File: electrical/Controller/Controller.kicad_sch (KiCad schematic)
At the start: 30 parts, among them J1 USB4145-03-0170-C, J3 TC2030-NL, U1 LP5912-3.3DRV, U2 USBLC6-2P6, U3 STM32L072CBTx

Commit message: Fix part selection for i2c pull-ups
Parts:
- R5, R6: LCSC C22939 -> C4190; Part UNI-ROYAL 0603WAF220KT5E -> UNI-ROYAL 0603WAF2201T5E
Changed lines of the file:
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@@
 			)
 		)
-		(property "Datasheet" "https://www.lcsc.com/datasheet/C22939.pdf"
+		(property "Datasheet" "https://www.lcsc.com/datasheet/C4190.pdf"
 			(at 281.94 149.86 0)
 			(effects
@@
 			)
 		)
-		(property "LCSC" "C22939"
+		(property "LCSC" "C4190"
 			(at 281.94 149.86 0)
 			(effects
@@
 			)
 		)
-		(property "Part" "UNI-ROYAL 0603WAF220KT5E"
+		(property "Part" "UNI-ROYAL 0603WAF2201T5E"
 			(at 281.94 149.86 0)
 			(effects
@@
 			)
 		)
-		(property "Datasheet" "https://www.lcsc.com/datasheet/C22939.pdf"
+		(property "Datasheet" "https://www.lcsc.com/datasheet/C4190.pdf"
 			(at 292.1 149.86 0)
 			(effects
@@
 			)
 		)
-		(property "LCSC" "C22939"
+		(property "LCSC" "C4190"
 			(at 292.1 149.86 0)
 			(effects
@@
 			)
 		)
-		(property "Part" "UNI-ROYAL 0603WAF220KT5E"
+		(property "Part" "UNI-ROYAL 0603WAF2201T5E"
 			(at 292.1 149.86 0)
 			(effects

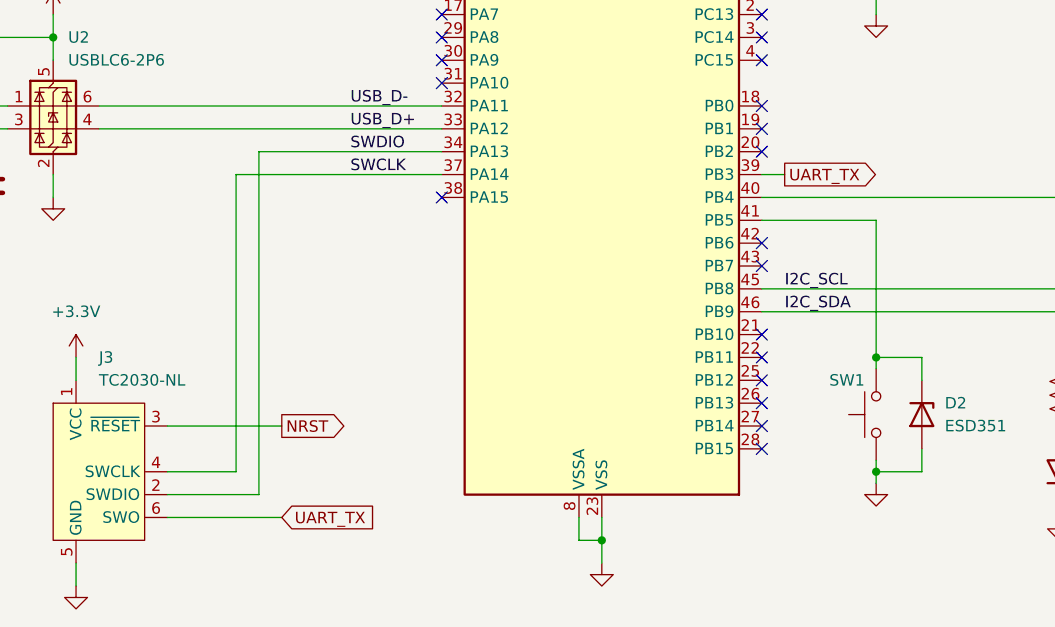
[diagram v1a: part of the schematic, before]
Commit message: Remove UART from debug connector
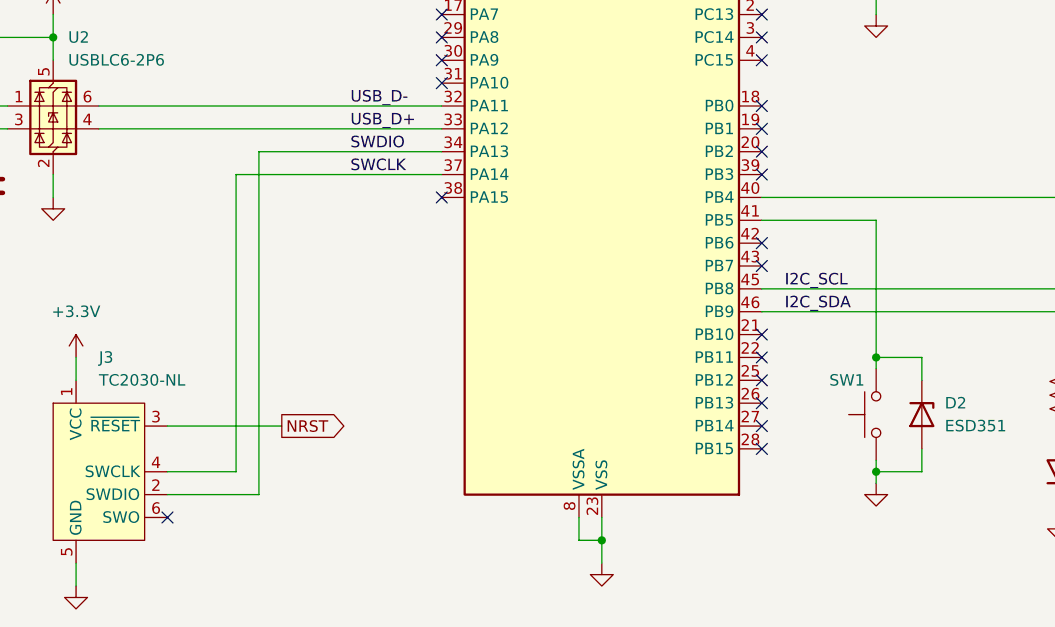
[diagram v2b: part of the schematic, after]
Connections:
- net UART_TX: no longer names the net of U3.39 (PB3)
- net UART_TX: no longer J3.6 (SWO)
- no-connect marks 31 -> 33
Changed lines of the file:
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@@
+	)
+	(no_connect
+		(at 233.68 143.51)
 	)
 	(no_connect
@@
 	)
 	(no_connect
+		(at 167.64 181.61)
+	)
+	(no_connect
 		(at 198.12 120.65)
 	)
@@
 	(wire
 		(pts
-			(xy 180.34 181.61) (xy 167.64 181.61)
-		)
-		(stroke
-			(width 0)
-			(type default)
-		)
-	)
-	(wire
-		(pts
 			(xy 121.92 134.62) (xy 121.92 140.97)
 		)
@@
 		(pts
 			(xy 167.64 171.45) (xy 180.34 171.45)
-		)
-		(stroke
-			(width 0)
-			(type default)
-		)
-	)
-	(wire
-		(pts
-			(xy 236.22 143.51) (xy 233.68 143.51)
 		)
 		(stroke
@@
 		)
 	)
-	(global_label "UART_TX"
-		(shape output)
-		(at 236.22 143.51 0)
-		(fields_autoplaced yes)
-		(effects
-			(font
-				(size 1.27 1.27)
-			)
-			(justify left)
-		)
-		(property "Intersheetrefs" "${INTERSHEET_REFS}"
-			(at 247.0066 143.51 0)
-			(effects
-				(font
-					(size 1.27 1.27)
-				)
-				(justify left)
-				(hide yes)
-			)
-		)
-	)
-	(global_label "UART_TX"
-		(shape input)
-		(at 180.34 181.61 0)
-		(fields_autoplaced yes)
-		(effects
-			(font
-				(size 1.27 1.27)
-			)
-			(justify left)
-		)
-		(property "Intersheetrefs" "${INTERSHEET_REFS}"
-			(at 191.1266 181.61 0)
-			(effects
-				(font
-					(size 1.27 1.27)
-				)
-				(justify left)
-				(hide yes)
-			)
-		)
-	)

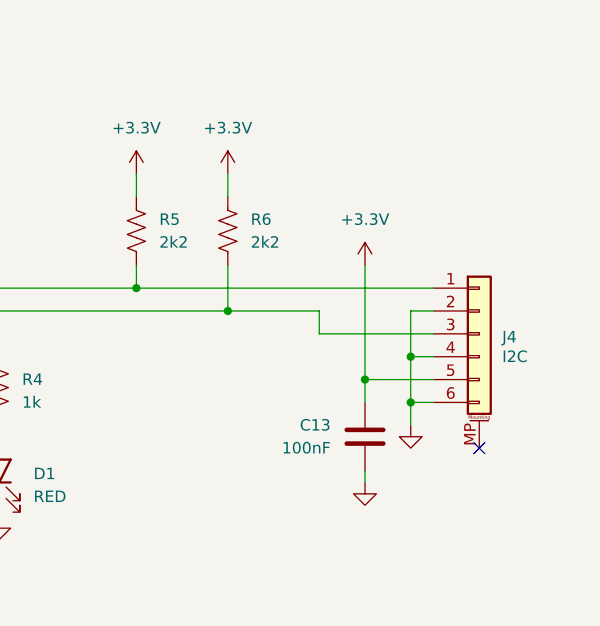
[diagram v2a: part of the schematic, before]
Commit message: Replace PicoBlade connectors with SKEDD
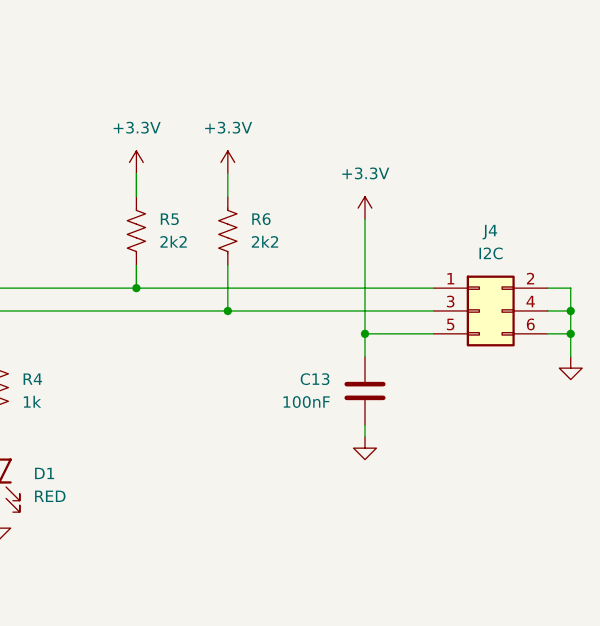
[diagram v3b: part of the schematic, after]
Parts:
- removed J4: ~, Connector_Molex:Molex_PicoBlade_53261-0671_1x06-1MP_P1.25mm_Horizontal, symbol Connector_Generic_MountingPin:Conn_01x06_MountingPin
- added J4: I2C, MidiConcertina:Wuerth_WR-WST_490107670612_2x03_P2.54mm_SKEDD, symbol Connector_Generic:Conn_02x03_Odd_Even
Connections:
- net +3.3V: now also J4.5 (Pin_5)
- net GND: now also J4.2 (Pin_2), J4.4 (Pin_4), J4.6 (Pin_6)
- net I2C_SCL: now also J4.1 (Pin_1)
- net I2C_SDA: now also J4.3 (Pin_3)
- no-connect marks 33 -> 32
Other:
- moved on the sheet: C13

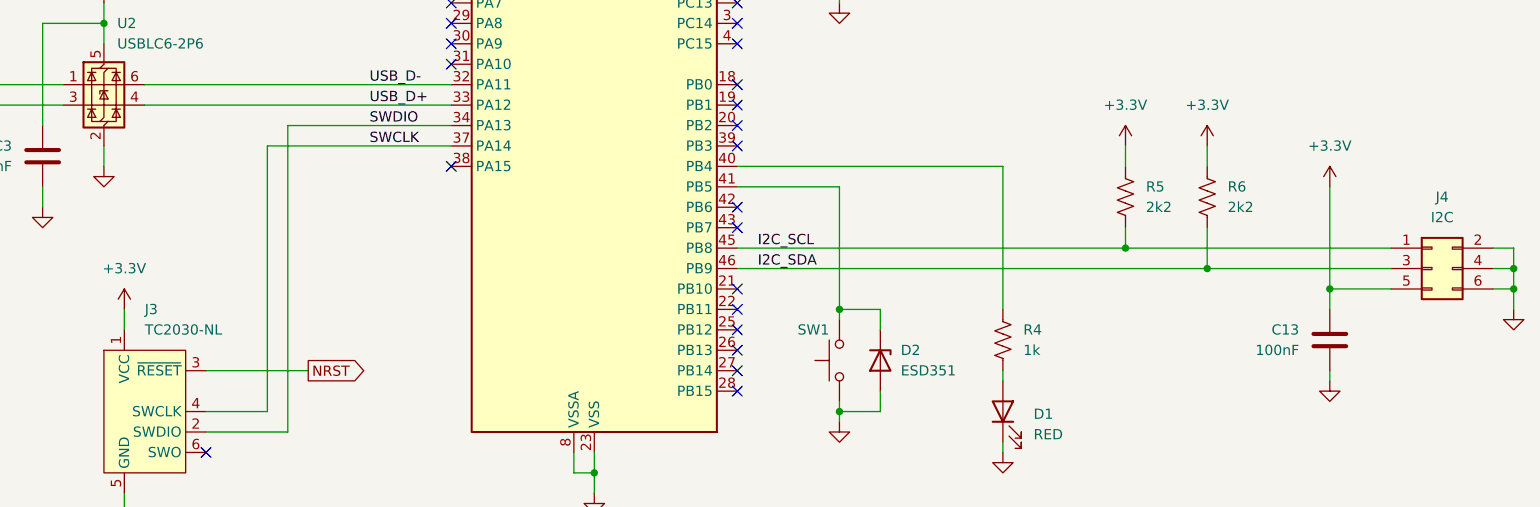
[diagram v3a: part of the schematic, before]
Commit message: Relabel components
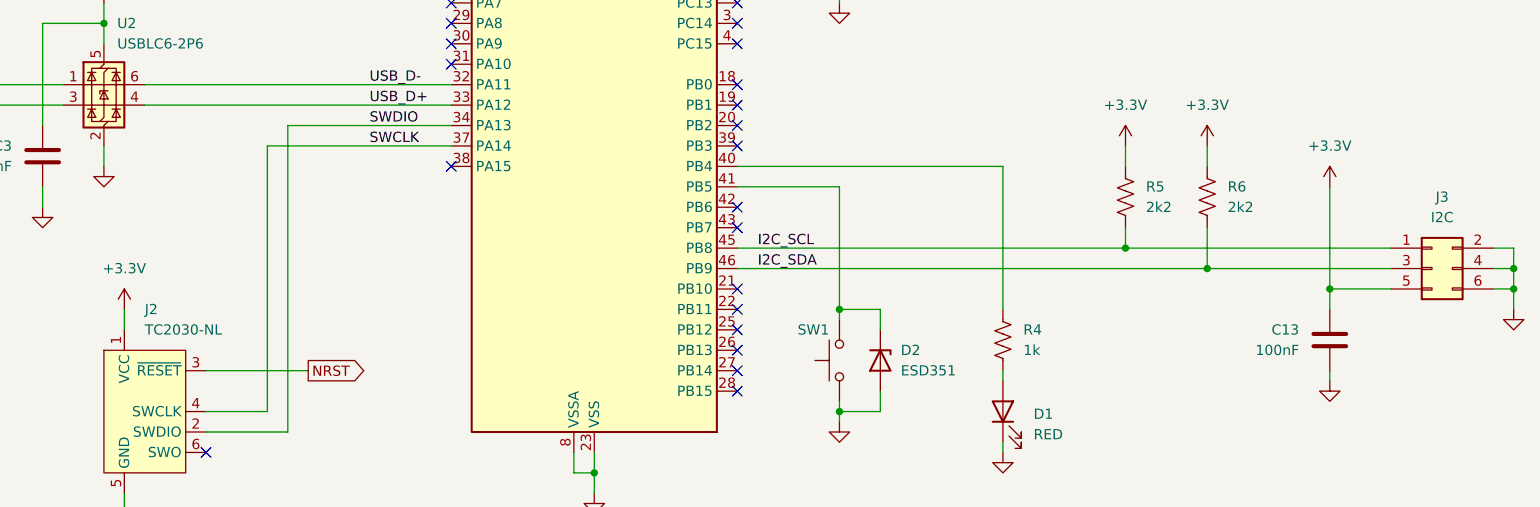
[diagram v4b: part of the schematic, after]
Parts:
- renumbered J3 to J2, J4 to J3
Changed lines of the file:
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@@
 		(dnp no)
 		(fields_autoplaced yes)
-		(property "Reference" "J4"
+		(property "Reference" "J3"
 			(at 321.31 149.86 0)
 			(effects
@@
 			(project ""
 				(path "/da26d94e-7a50-4b99-9678-5aaaf6987a15"
-					(reference "J4")
+					(reference "J3")
 					(unit 1)
 				)
@@
 		(on_board yes)
 		(dnp no)
-		(property "Reference" "J3"
+		(property "Reference" "J2"
 			(at 160.02 163.83 0)
 			(effects
@@
 			(project "control"
 				(path "/da26d94e-7a50-4b99-9678-5aaaf6987a15"
-					(reference "J3")
-					(unit 1)
-				)
+					(reference "J2")
+					(unit 1)
+				)

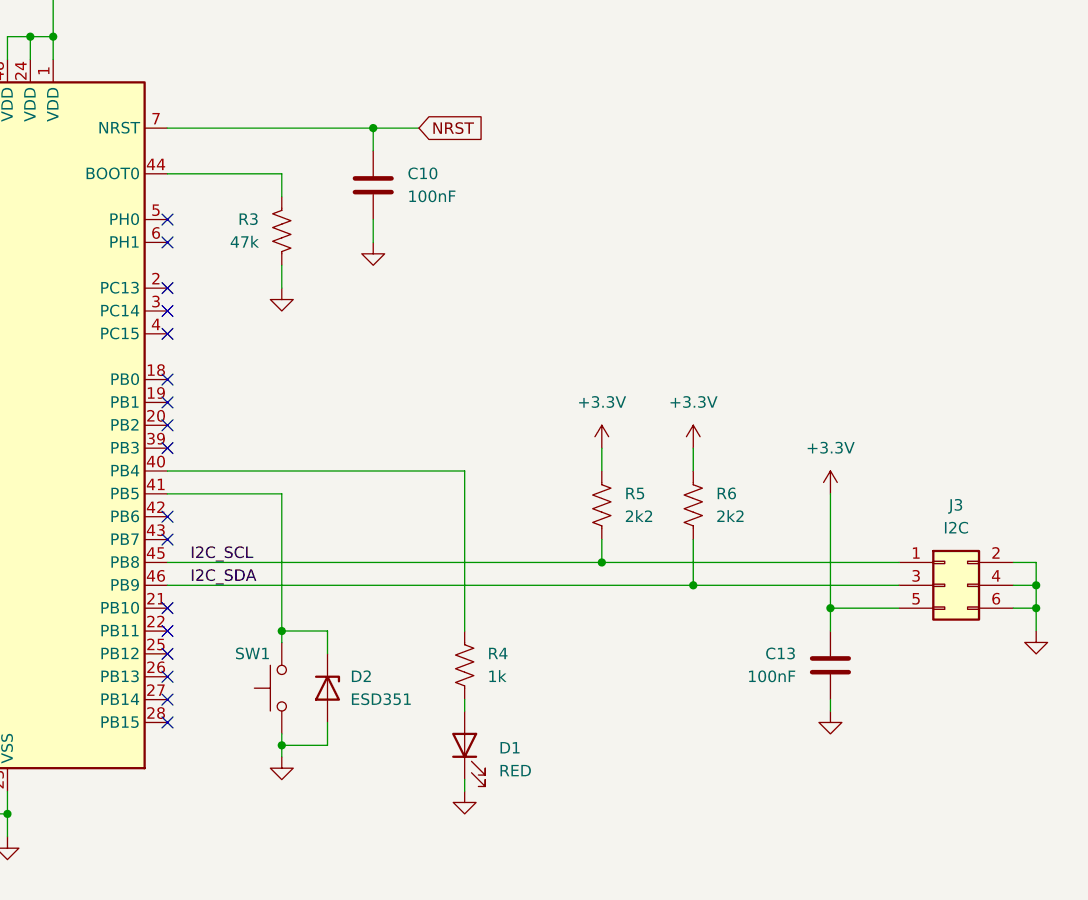
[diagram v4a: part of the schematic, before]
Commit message: Add gpio-controlled switch for i2c bus power
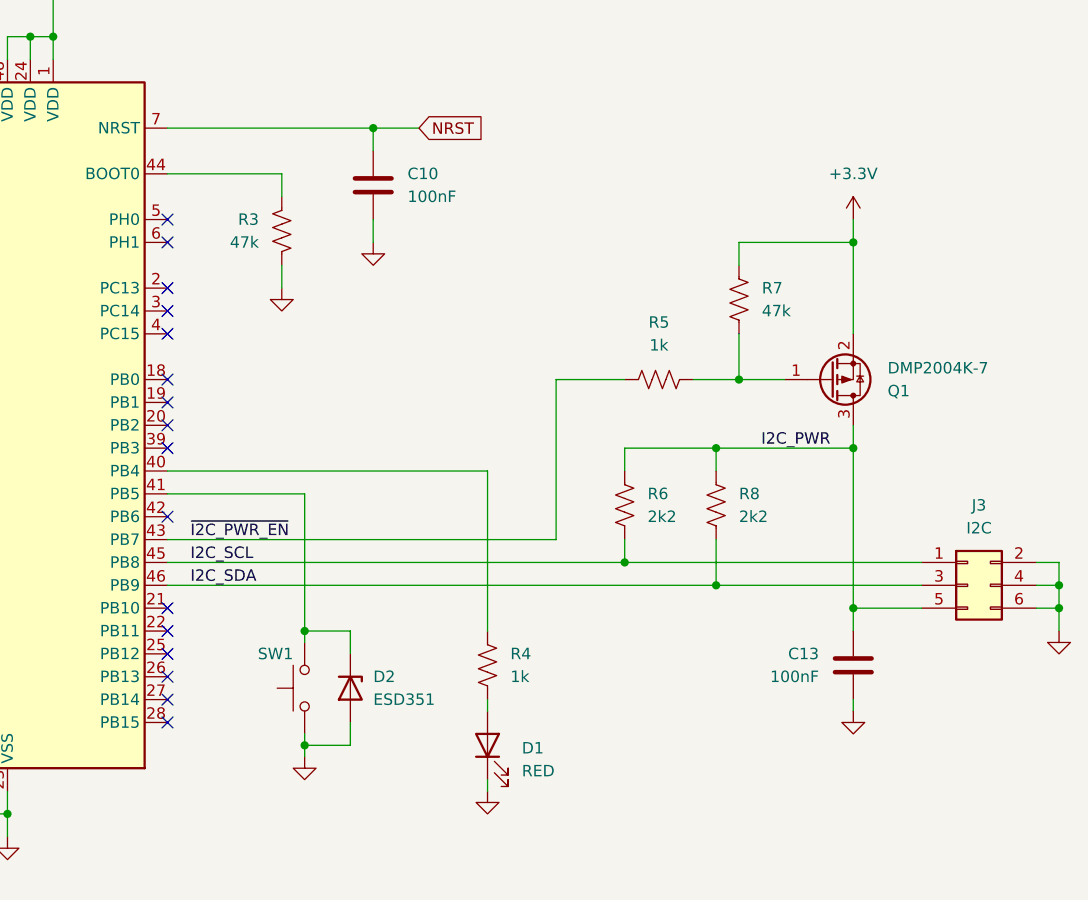
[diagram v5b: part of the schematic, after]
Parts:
- added Q1: DMP2004K-7, Package_TO_SOT_SMD:SOT-23, symbol Transistor_FET:Q_PMOS_GSD
- added R5: 1k, Resistor_SMD:R_0402_1005Metric, symbol Device:R_US
- added R7: 47k, Resistor_SMD:R_0402_1005Metric, symbol Device:R_US
- renumbered R5 to R6, R6 to R8
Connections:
- net +3.3V: now also Q1.2 (S), R7.1; no longer C13.1, J3.5 (Pin_5), R6.1, R8.1
- net ~{I2C_PWR_EN}: now reaches U3.43 (PB7)
- net ~{I2C_PWR_EN}: now also R5.1
- new net: Q1.1 (G), R5.2, R7.2
- new net I2C_PWR: C13.1, J3.5 (Pin_5), Q1.3 (D), R6.1, R8.1
- no-connect marks 32 -> 31
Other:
- moved on the sheet: C13, D1, D2, J3, R4, R6, R8, SW1
